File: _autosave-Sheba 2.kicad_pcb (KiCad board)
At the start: 2 copper layers, 85.7 x 54 mm, 69 parts, among them J1 Conn_01x02_Pin, J2 Conn_02x04_Top_Bottom, J3 Conn_01x06_Pin, J4 Conn_01x03_Pin, J5 Conn_01x03_Pin, J6 Conn_01x03_Pin, P1 USB 2.0 Type-C Port, SW1 SPDT Switch, U1 STM32F072CBTx, U2 MIC5504-3.3YM5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

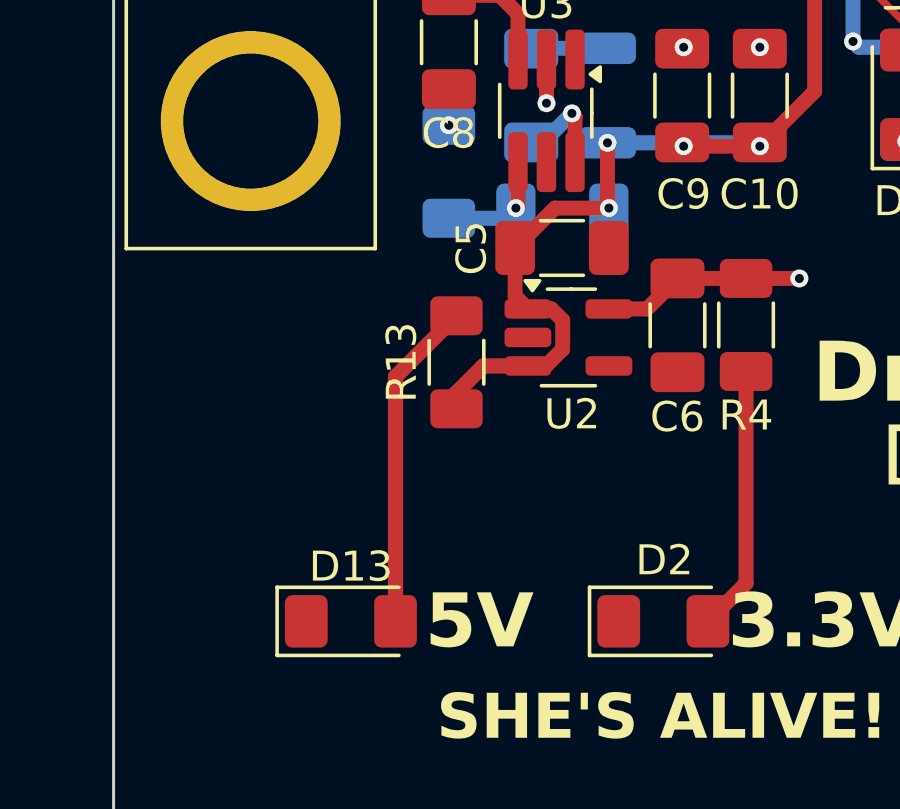
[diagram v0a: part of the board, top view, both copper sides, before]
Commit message: ig we switching to esp32 now
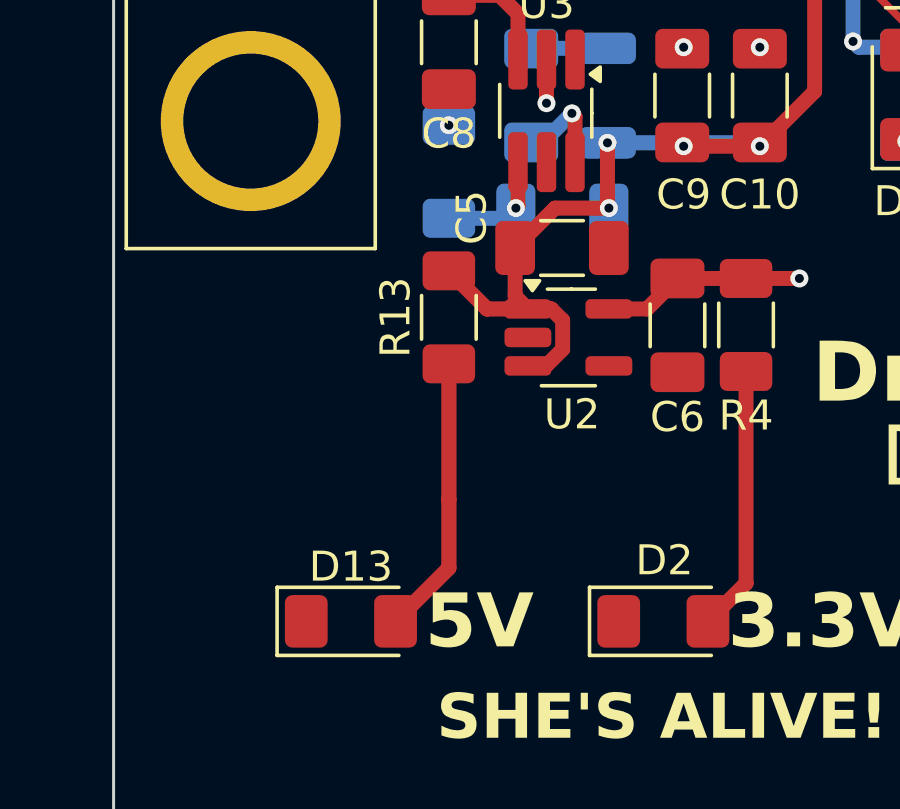
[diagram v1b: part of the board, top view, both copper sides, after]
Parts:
- moved R13 1.52 mm to (64.5, 55.4), turned to -90 degrees
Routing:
- net Net-(D13-A): track 11.0 -> 9.32 mm
